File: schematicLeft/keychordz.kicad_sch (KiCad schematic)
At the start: 41 parts, among them IC1 MCP73833-BZI_UN, J1 USB_C_Receptacle_USB2.0, J2 Conn_01x04_Male, J3 Conn_01x04_Male, SW1 SW_Push, SW2 SW_Push, SW3 SW_Push, SW4 SW_Push, SW5 SW_Push, SW6 SW_Push, SW7 SW_Push, SW9 SW_SPST, U1 nRF52840_Breakout

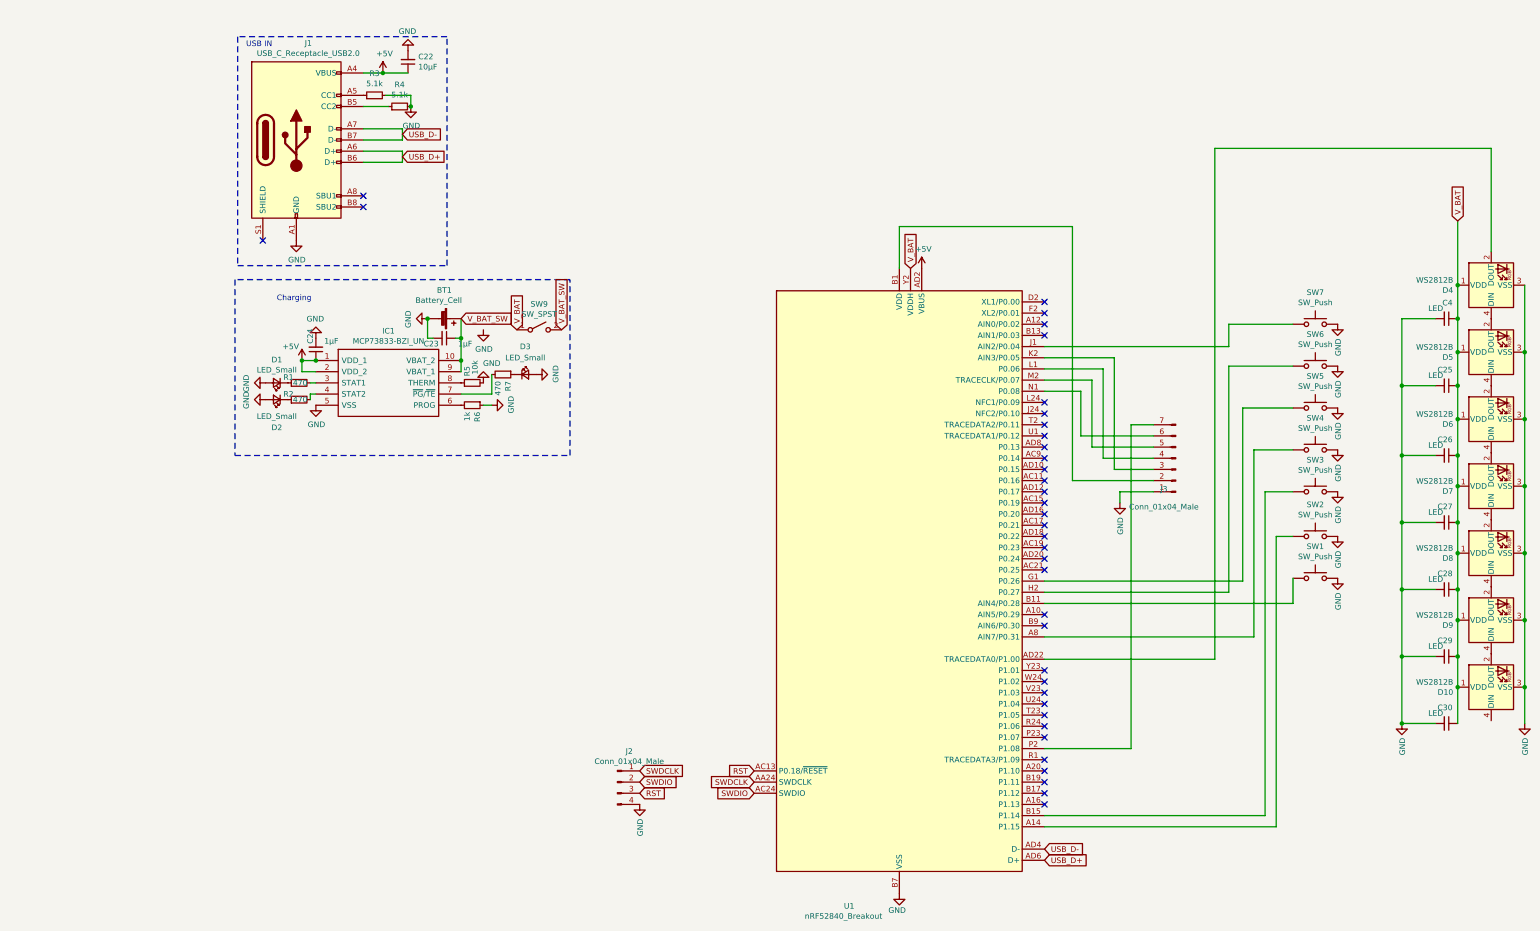
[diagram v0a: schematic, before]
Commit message: change left PCB to STM32
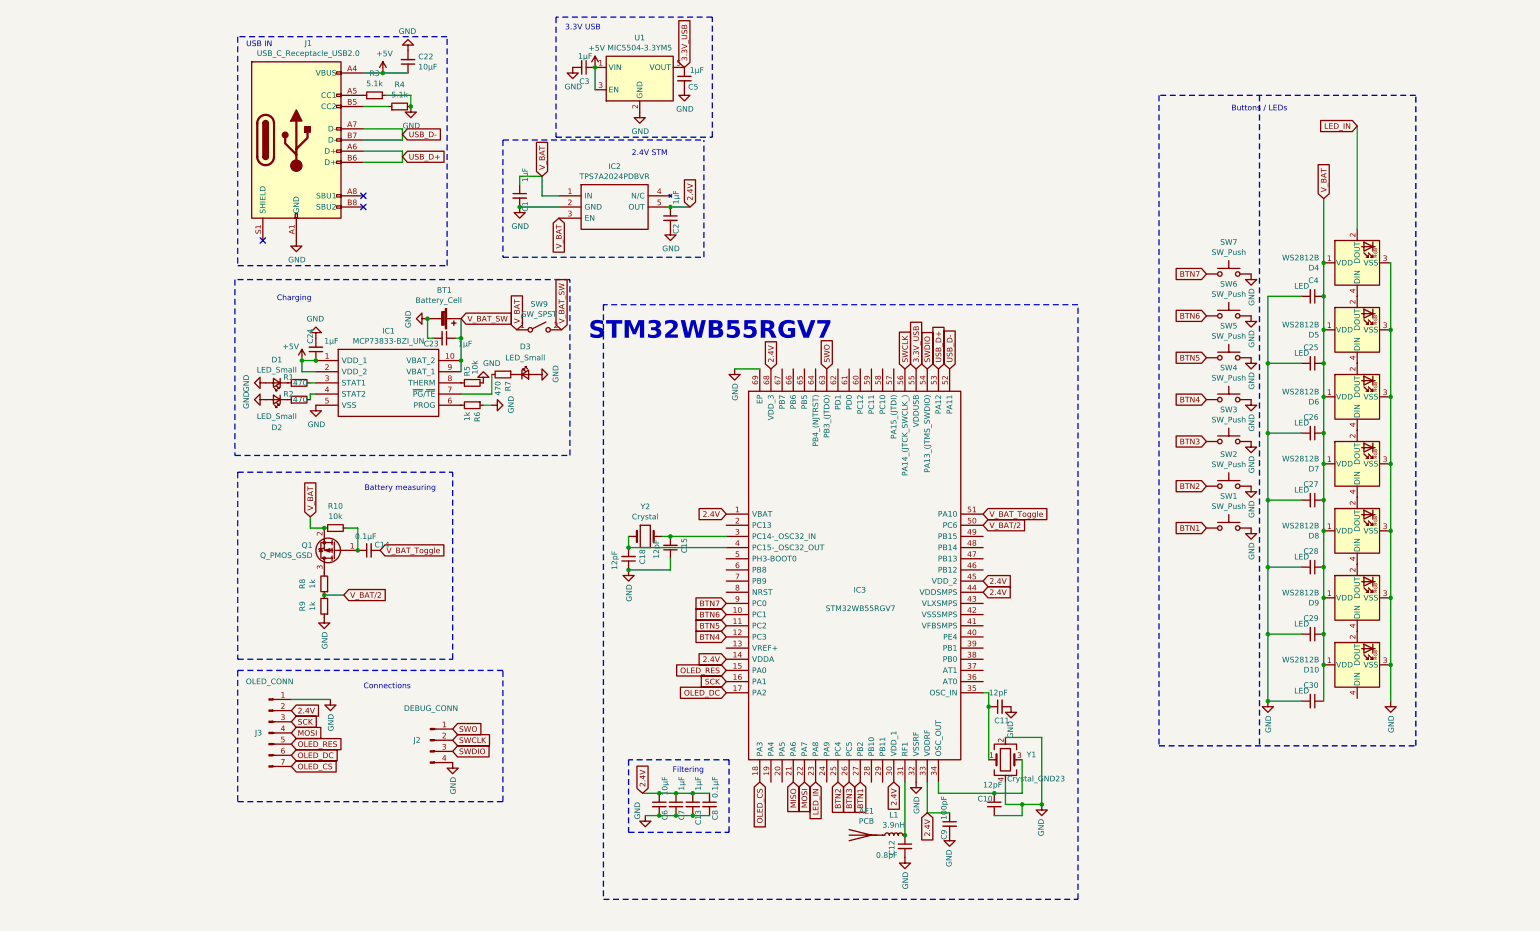
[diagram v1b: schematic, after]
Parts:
- removed U1: nRF52840_Breakout, schematic:nRF52840_Breakout, symbol MCU_Nordic:nRF52840_Breakout
- added AE1: PCB, RF_Antenna:Texas_SWRA117D_2.4GHz_Right, symbol Device:Antenna
- added C1, C13, C2, C3, C5, C7: 1µF, Capacitor_SMD:C_0402_1005Metric_Pad0.74x0.62mm_HandSolder, symbol Device:C_Small
- added C10, C11, C15, C18: 12pF, Capacitor_SMD:C_0603_1608Metric_Pad1.08x0.95mm_HandSolder, symbol Device:C_Small
- added C12: 0.8pF, Capacitor_SMD:C_0201_0603Metric_Pad0.64x0.40mm_HandSolder, symbol Device:C_Small
- added C14, C8: 0.1µF, Capacitor_SMD:C_0402_1005Metric_Pad0.74x0.62mm_HandSolder, symbol Device:C_Small
- added C6: 10µF, Capacitor_SMD:C_0402_1005Metric_Pad0.74x0.62mm_HandSolder, symbol Device:C_Small
- added C9: 100pF, Capacitor_SMD:C_0402_1005Metric_Pad0.74x0.62mm_HandSolder, symbol Device:C_Small
- added IC2: TPS7A2024PDBVR, SamacSys_Parts:SOT95P280X145-5N, symbol LoaderParts:TPS7A2033PDBVR
- added IC3: STM32WB55RGV7, SamacSys_Parts:QFN40P800X800X100-69N-D, symbol LoaderParts:STM32WB55RGV7
- added L1: 3.9nH, Inductor_SMD:L_0402_1005Metric_Pad0.77x0.64mm_HandSolder, symbol Device:L_Small
- added Q1: Q_PMOS_GSD, Package_TO_SOT_SMD:SC-59_Handsoldering, symbol Device:Q_PMOS_GSD
- added R10: 10k, Resistor_SMD:R_0603_1608Metric_Pad0.98x0.95mm_HandSolder, symbol Device:R_Small
- added R8, R9: 1k, Resistor_SMD:R_0603_1608Metric_Pad0.98x0.95mm_HandSolder, symbol Device:R_Small
- added U1: MIC5504-3.3YM5, Package_TO_SOT_SMD:SOT-23-5, symbol Regulator_Linear:MIC5504-3.3YM5
- added Y1: Crystal_GND23, Crystal:Crystal_SMD_2016-4Pin_2.0x1.6mm_HandSoldering, symbol Device:Crystal_GND24
- added Y2: Crystal, Crystal:Crystal_SMD_MicroCrystal_CC7V-T1A-2Pin_3.2x1.5mm_HandSoldering, symbol Device:Crystal
- J2: value Conn_01x04_Male -> DEBUG_CONN
- J3: value Conn_01x04_Male -> OLED_CONN
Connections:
- net RST is gone; now on net SWDIO: J2.3 (Pin_3)
- net +5V: now also C3.1, U1.1 (VIN), U1.3 (EN)
- net GND: now also C1.2, C10.2, C11.2, C12.2, C13.2, C15.1, C18.1, C2.2, C3.2, C5.2, C6.2, C7.2, C8.2, C9.2, IC2.2 (GND), IC3.32 (VSSRF), IC3.69 (EP), R9.1, U1.2 (GND), Y1.2, Y1.4
- net SWDIO: now also IC3.54 (PA13_(JTMS_SWDIO)); no longer J2.2 (Pin_2)
- net USB_D+: now also IC3.53 (PA12)
- net USB_D-: now also IC3.52 (PA11)
- net V_BAT: now also C1.1, IC2.1 (IN), IC2.3 (EN), Q1.2 (S), R10.1
- net BTN5: now reaches SW5.1
- net BTN5: now also IC3.11 (PC2)
- net BTN4: now reaches SW4.1
- net BTN4: now also IC3.12 (PC3)
- net BTN3: now reaches SW3.1
- net BTN3: now also IC3.26 (PC5)
- net BTN2: now reaches SW2.1
- net BTN2: now also IC3.25 (PC4)
- net BTN1: now reaches SW1.1
- net BTN1: now also IC3.27 (PB2)
- net 2.4V: now reaches J3.2 (Pin_2)
- net 2.4V: now also C13.1, C2.1, C6.1, C7.1, C8.1, C9.1, IC2.5 (OUT), IC3.1 (VBAT), IC3.14 (VDDA), IC3.30 (VDD_1), IC3.33 (VDDRF), IC3.44 (VDDSMPS), IC3.45 (VDD_2), IC3.68 (VDD_3)
- net SCK: now reaches J3.3 (Pin_3)
- net SCK: now also IC3.16 (PA1)
- net MOSI: now reaches J3.4 (Pin_4)
- net MOSI: now also IC3.22 (PA7)
- net OLED_RES: now reaches J3.5 (Pin_5)
- net OLED_RES: now also IC3.15 (PA0)
- net OLED_DC: now reaches J3.6 (Pin_6)
- net OLED_DC: now also IC3.17 (PA2)
- net OLED_CS: now reaches J3.7 (Pin_7)
- net OLED_CS: now also IC3.18 (PA3)
- net BTN6: now reaches SW6.1
- net BTN6: now also IC3.10 (PC1)
- net LED_IN: now reaches D4.2 (DOUT)
- net LED_IN: now also IC3.23 (PA8)
- net BTN7: now reaches SW7.1
- net BTN7: now also IC3.9 (PC0)
- net SWDCLK renamed SWO
- net SWO: now also IC3.63 (PB3_(JTDO))
- new net: C12.1, IC3.31 (RF1), L1.2
- new net: C14.1, Q1.1 (G), R10.2
- new net: C15.2, IC3.3 (PC14-_OSC32_IN), Y2.2
- new net: C10.1, IC3.34 (OSC_OUT), Y1.3
- new net: C11.1, IC3.35 (OSC_IN), Y1.1
- new net: C18.2, IC3.4 (PC15-_OSC32_OUT), Y2.1
- new net: Q1.3 (D), R8.2
- new net: AE1.1 (A), L1.1
- new net 3.3V_USB: C5.1, IC3.55 (VDDUSB), U1.5 (VOUT)
- new net MISO: IC3.21 (PA6)
- new net SWCLK: IC3.56 (PA14_(JTCK_SWCLK_)), J2.2 (Pin_2)
- new net V_BAT_Toggle: C14.2, IC3.51 (PA10)
- new net V_BAT/2: IC3.50 (PC6), R8.1, R9.2
- no-connect marks 37 -> 3
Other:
- note added: "2.4V STM"
- note added: "3.3V USB"
- note added: "Battery measuring"
- note added: "Buttons / LEDs"
- note added: "Connections"
- note added: "Filtering"
- note added: "STM32WB55RGV7"
- moved on the sheet: C25, C26, C27, C28, C29, C30, C4, D10, D4, D5, D6, D7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

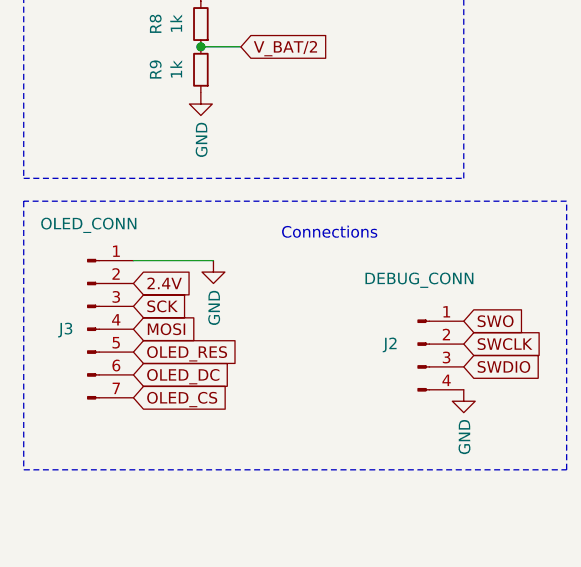
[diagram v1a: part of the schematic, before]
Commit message: change OLED voltage to V_BAT (ordered this commit)
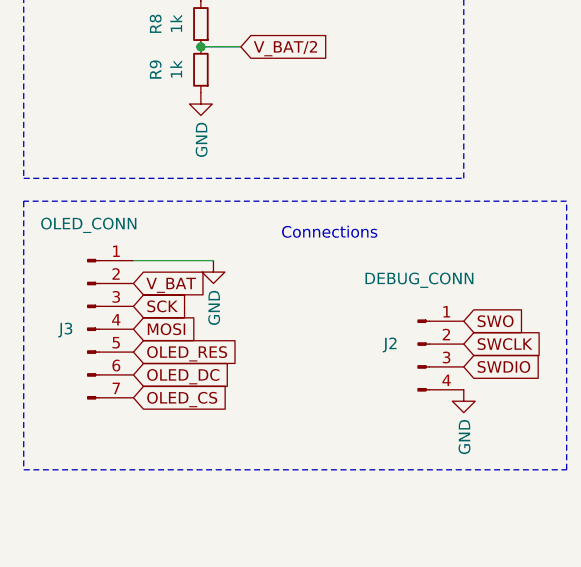
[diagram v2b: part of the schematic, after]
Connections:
- net 2.4V: no longer J3.2 (Pin_2)
- net V_BAT: now also J3.2 (Pin_2)
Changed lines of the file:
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@@
     (effects (font (size 1.27 1.27)) (justify right bottom))
   )
-  (global_label "2.4V" (shape input) (at 29.972 170.434 0)
+  (global_label "V_BAT" (shape input) (at 29.972 170.434 0)
     (effects (font (size 1.27 1.27)) (justify left))
-    (property "Intersheet References" "${INTERSHEET_REFS}" (id 0) (at 36.4975 170.5134 0)
+    (property "Intersheet References" "${INTERSHEET_REFS}" (id 0) (at 37.7675 170.3546 0)
       (effects (font (size 1.27 1.27)) (justify left) hide)
     )

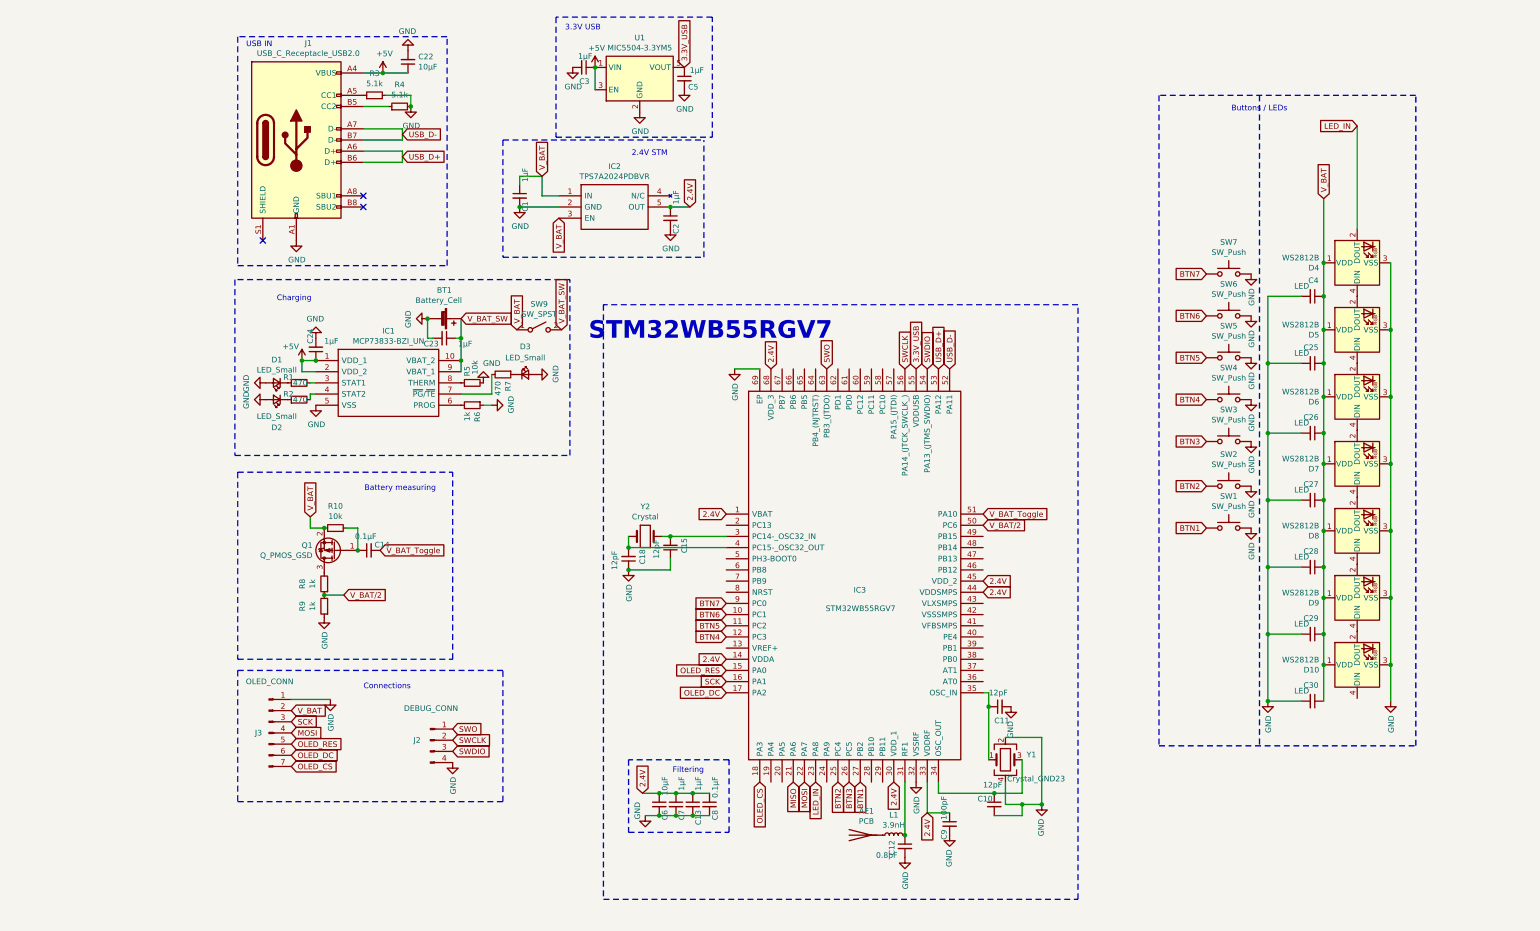
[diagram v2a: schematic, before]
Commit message: use Arduino pro micro
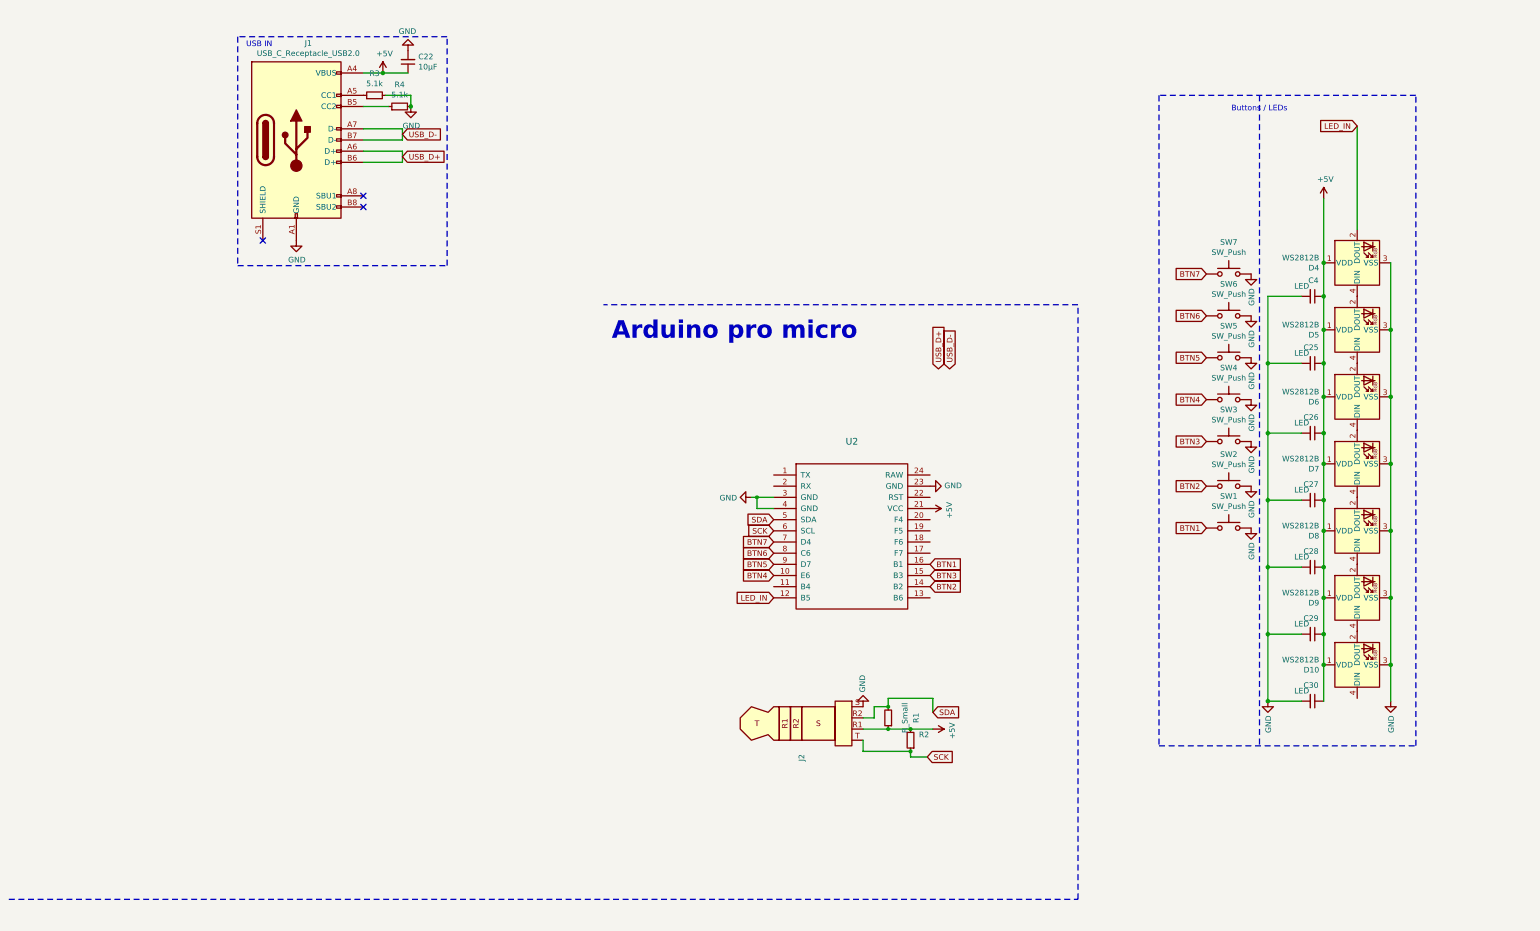
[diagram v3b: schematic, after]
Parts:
- removed AE1: PCB, RF_Antenna:Texas_SWRA117D_2.4GHz_Right, symbol Device:Antenna
- removed BT1: Battery_Cell, Battery:BatteryHolder_MPD_BH-18650-PC2, symbol Device:Battery_Cell
- removed C1, C13, C2, C23, C24, C3, C5, C7: 1µF, Capacitor_SMD:C_0402_1005Metric_Pad0.74x0.62mm_HandSolder, symbol Device:C_Small
- removed C10, C11, C15, C18: 12pF, Capacitor_SMD:C_0603_1608Metric_Pad1.08x0.95mm_HandSolder, symbol Device:C_Small
- removed C12: 0.8pF, Capacitor_SMD:C_0201_0603Metric_Pad0.64x0.40mm_HandSolder, symbol Device:C_Small
- removed C14, C8: 0.1µF, Capacitor_SMD:C_0402_1005Metric_Pad0.74x0.62mm_HandSolder, symbol Device:C_Small
- removed C6: 10µF, Capacitor_SMD:C_0402_1005Metric_Pad0.74x0.62mm_HandSolder, symbol Device:C_Small
- removed C9: 100pF, Capacitor_SMD:C_0402_1005Metric_Pad0.74x0.62mm_HandSolder, symbol Device:C_Small
- removed D1, D2, D3: LED_Small, LED_SMD:LED_0603_1608Metric_Pad1.05x0.95mm_HandSolder, symbol Device:LED_Small
- removed IC1: MCP73833-BZI_UN, Package_SO:MSOP-10_3x3mm_P0.5mm, symbol LoaderParts:MCP73833-BZI_UN
- removed IC2: TPS7A2024PDBVR, SamacSys_Parts:SOT95P280X145-5N, symbol LoaderParts:TPS7A2033PDBVR
- removed IC3: STM32WB55RGV7, SamacSys_Parts:QFN40P800X800X100-69N-D, symbol LoaderParts:STM32WB55RGV7
- removed J2: DEBUG_CONN, Connector_PinHeader_2.54mm:PinHeader_1x04_P2.54mm_Vertical, symbol Connector:Conn_01x04_Male
- removed J3: OLED_CONN, Connector_PinHeader_2.54mm:PinHeader_1x07_P2.54mm_Vertical, symbol Connector:Conn_01x07_Male
- removed L1: 3.9nH, Inductor_SMD:L_0402_1005Metric_Pad0.77x0.64mm_HandSolder, symbol Device:L_Small
- removed Q1: Q_PMOS_GSD, Package_TO_SOT_SMD:SC-59_Handsoldering, symbol Device:Q_PMOS_GSD
- removed R10: 10k, Resistor_SMD:R_0603_1608Metric_Pad0.98x0.95mm_HandSolder, symbol Device:R_Small
- removed R5: 10k, Resistor_SMD:R_0402_1005Metric_Pad0.72x0.64mm_HandSolder, symbol Device:R_Small
- removed R6: 1k, Resistor_SMD:R_0402_1005Metric_Pad0.72x0.64mm_HandSolder, symbol Device:R_Small
- removed R7: 470, Resistor_SMD:R_0603_1608Metric_Pad0.98x0.95mm_HandSolder, symbol Device:R_Small
- removed R8, R9: 1k, Resistor_SMD:R_0603_1608Metric_Pad0.98x0.95mm_HandSolder, symbol Device:R_Small
- removed SW9: SW_SPST, Button_Switch_THT:SW_DIP_SPSTx02_Slide_6.7x6.64mm_W7.62mm_P2.54mm_LowProfile, symbol Switch:SW_SPST
- removed U1: MIC5504-3.3YM5, Package_TO_SOT_SMD:SOT-23-5, symbol Regulator_Linear:MIC5504-3.3YM5
- removed Y1: Crystal_GND23, Crystal:Crystal_SMD_2016-4Pin_2.0x1.6mm_HandSoldering, symbol Device:Crystal_GND24
- removed Y2: Crystal, Crystal:Crystal_SMD_MicroCrystal_CC7V-T1A-2Pin_3.2x1.5mm_HandSoldering, symbol Device:Crystal
- added J2: (no value), symbol Connector:AudioPlug4
- added U2: (no value), symbol promicro:ProMicro
- R1: value 470 -> R_Small; footprint Resistor_SMD:R_0603_1608Metric_Pad0.98x0.95mm_HandSolder -> (none)
- R2: value 470 -> (none); footprint Resistor_SMD:R_0603_1608Metric_Pad0.98x0.95mm_HandSolder -> (none)
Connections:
- net V_BAT is gone; now on net +5V: C25.1, C26.1, C27.1, C28.1, C29.1, C30.1, C4.1, D10.1 (VDD), D4.1 (VDD), D5.1 (VDD), D6.1 (VDD), D7.1 (VDD), D8.1 (VDD), D9.1 (VDD)
- net +5V: now also R1.1, R2.2, J2.R1, U2.21 (VCC)
- net BTN1: now also U2.16 (B1)
- net BTN2: now also U2.14 (B2)
- net BTN3: now also U2.15 (B3)
- net BTN4: now also U2.10 (E6)
- net BTN5: now also U2.9 (D7)
- net BTN6: now also U2.8 (C6)
- net BTN7: now also U2.7 (D4)
- net GND: now also J2.S, U2.23 (GND), U2.3 (GND), U2.4 (GND)
- net LED_IN: now also U2.12 (B5)
- net SCK: now also R2.1, J2.T, U2.6 (SCL)
- net SDA: now reaches R1.2
- net SDA: now also J2.R2, U2.5 (SDA)
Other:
- note added: "Arduino pro micro"
- note removed: "2.4V STM"
- note removed: "3.3V USB"
- note removed: "Battery measuring"
- note removed: "Charging"
- note removed: "Connections"
- note removed: "Filtering"
- note removed: "STM32WB55RGV7"
